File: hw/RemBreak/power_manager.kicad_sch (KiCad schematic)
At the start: 20 parts, among them IC1 LTC2943IDD#TRPBF, J4 Screw_Terminal_01x02, J5 Conn_01x03_MountingPin, Q1 BC337, Q2 BC847, U1 INA219BxDCN, U2 MAX40200AUK

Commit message: routing in progress added new subsheet to easily swap signals at the control connector
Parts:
- renumbered J4 to J3, J5 to J4
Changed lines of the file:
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@@
 		(dnp no)
 		(fields_autoplaced yes)
-		(property "Reference" "#PWR013"
+		(property "Reference" "#PWR010"
 			(at 116.84 69.85 0)
 			(effects
@@
 			(project "RemBreak"
 				(path "/e6d4ae5b-c9d7-4cbe-b288-c929fdf55a75/65dd8b54-1c0a-4683-aa46-51c439d49612"
-					(reference "#PWR013")
+					(reference "#PWR010")
 					(unit 1)
 				)
@@
 		(dnp no)
 		(fields_autoplaced yes)
-		(property "Reference" "#PWR018"
+		(property "Reference" "#PWR015"
 			(at 212.09 146.05 0)
 			(effects
@@
 			(project "RemBreak"
 				(path "/e6d4ae5b-c9d7-4cbe-b288-c929fdf55a75/65dd8b54-1c0a-4683-aa46-51c439d49612"
-					(reference "#PWR018")
+					(reference "#PWR015")
 					(unit 1)
 				)
@@
 		(on_board yes)
 		(dnp no)
-		(property "Reference" "J4"
+		(property "Reference" "J3"
 			(at 23.622 78.74 0)
 			(effects
@@
 			(project "RemBreak"
 				(path "/e6d4ae5b-c9d7-4cbe-b288-c929fdf55a75/65dd8b54-1c0a-4683-aa46-51c439d49612"
-					(reference "J4")
+					(reference "J3")
 					(unit 1)
 				)
@@
 		(dnp no)
 		(fields_autoplaced yes)
-		(property "Reference" "#PWR015"
+		(property "Reference" "#PWR012"
 			(at 190.5 74.93 0)
 			(effects
@@
 			(project ""
 				(path "/e6d4ae5b-c9d7-4cbe-b288-c929fdf55a75/65dd8b54-1c0a-4683-aa46-51c439d49612"
-					(reference "#PWR015")
+					(reference "#PWR012")
 					(unit 1)
 				)
@@
 		(dnp no)
 		(fields_autoplaced yes)
-		(property "Reference" "#PWR016"
+		(property "Reference" "#PWR013"
 			(at 200.66 78.74 0)
 			(effects
@@
 			(project ""
 				(path "/e6d4ae5b-c9d7-4cbe-b288-c929fdf55a75/65dd8b54-1c0a-4683-aa46-51c439d49612"
-					(reference "#PWR016")
+					(reference "#PWR013")
 					(unit 1)
 				)
@@
 		(dnp no)
 		(fields_autoplaced yes)
-		(property "Reference" "#PWR011"
+		(property "Reference" "#PWR08"
 			(at 80.01 144.78 0)
 			(effects
@@
 			(project "RemBreak"
 				(path "/e6d4ae5b-c9d7-4cbe-b288-c929fdf55a75/65dd8b54-1c0a-4683-aa46-51c439d49612"
-					(reference "#PWR011")
+					(reference "#PWR08")
 					(unit 1)
 				)
@@
 		(dnp no)
 		(fields_autoplaced yes)
-		(property "Reference" "#PWR010"
+		(property "Reference" "#PWR07"
 			(at 60.96 54.61 0)
 			(effects
@@
 			(project "RemBreak"
 				(path "/e6d4ae5b-c9d7-4cbe-b288-c929fdf55a75/65dd8b54-1c0a-4683-aa46-51c439d49612"
-					(reference "#PWR010")
+					(reference "#PWR07")
 					(unit 1)
 				)
@@
 		(on_board yes)
 		(dnp no)
-		(property "Reference" "J5"
+		(property "Reference" "J4"
 			(at 24.892 90.17 0)
 			(effects
@@
 			(project ""
 				(path "/e6d4ae5b-c9d7-4cbe-b288-c929fdf55a75/65dd8b54-1c0a-4683-aa46-51c439d49612"
-					(reference "J5")
+					(reference "J4")
 					(unit 1)
 				)
@@
 		(dnp no)
 		(fields_autoplaced yes)
-		(property "Reference" "#PWR09"
+		(property "Reference" "#PWR06"
 			(at 54.61 71.12 0)
 			(effects
@@
 			(project "RemBreak"
 				(path "/e6d4ae5b-c9d7-4cbe-b288-c929fdf55a75/65dd8b54-1c0a-4683-aa46-51c439d49612"
-					(reference "#PWR09")
+					(reference "#PWR06")
 					(unit 1)
 				)
@@
 		(dnp no)
 		(fields_autoplaced yes)
-		(property "Reference" "#PWR017"
+		(property "Reference" "#PWR014"
 			(at 207.01 34.29 0)
 			(effects
@@
 			(project "RemBreak"
 				(path "/e6d4ae5b-c9d7-4cbe-b288-c929fdf55a75/65dd8b54-1c0a-4683-aa46-51c439d49612"
-					(reference "#PWR017")
+					(reference "#PWR014")
 					(unit 1)
 				)
@@
 		(dnp no)
 		(fields_autoplaced yes)
-		(property "Reference" "#PWR014"
+		(property "Reference" "#PWR011"
 			(at 158.75 85.09 0)
 			(effects
@@
 			(project "RemBreak"
 				(path "/e6d4ae5b-c9d7-4cbe-b288-c929fdf55a75/65dd8b54-1c0a-4683-aa46-51c439d49612"
-					(reference "#PWR014")
+					(reference "#PWR011")
 					(unit 1)
 				)
@@
 		(dnp no)
 		(fields_autoplaced yes)
-		(property "Reference" "#PWR012"
+		(property "Reference" "#PWR09"
 			(at 92.71 124.46 0)
 			(effects
@@
 			(project "RemBreak"
 				(path "/e6d4ae5b-c9d7-4cbe-b288-c929fdf55a75/65dd8b54-1c0a-4683-aa46-51c439d49612"
-					(reference "#PWR012")
+					(reference "#PWR09")
 					(unit 1)
 				)
@@
 		(dnp no)
 		(fields_autoplaced yes)
-		(property "Reference" "#PWR07"
+		(property "Reference" "#PWR04"
 			(at 39.37 101.6 0)
 			(effects
@@
 			(project ""
 				(path "/e6d4ae5b-c9d7-4cbe-b288-c929fdf55a75/65dd8b54-1c0a-4683-aa46-51c439d49612"
-					(reference "#PWR07")
+					(reference "#PWR04")
 					(unit 1)
 				)
@@
 		(dnp no)
 		(fields_autoplaced yes)
-		(property "Reference" "#PWR08"
+		(property "Reference" "#PWR05"
 			(at 41.91 134.62 0)
 			(effects
@@
 			(project "RemBreak"
 				(path "/e6d4ae5b-c9d7-4cbe-b288-c929fdf55a75/65dd8b54-1c0a-4683-aa46-51c439d49612"
-					(reference "#PWR08")
+					(reference "#PWR05")
 					(unit 1)
 				)
@@
 		(dnp no)
 		(fields_autoplaced yes)
-		(property "Reference" "#PWR019"
+		(property "Reference" "#PWR016"
 			(at 236.22 146.05 0)
 			(effects
@@
 			(project "RemBreak"
 				(path "/e6d4ae5b-c9d7-4cbe-b288-c929fdf55a75/65dd8b54-1c0a-4683-aa46-51c439d49612"
-					(reference "#PWR019")
-					(unit 1)
-				)
+					(reference "#PWR016")
+					(unit 1)
+				)

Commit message: changed board settings and replaced r and c footprints with the ones for handsoldering
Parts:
- C1: footprint Capacitor_SMD:C_0805_2012Metric -> Capacitor_SMD:C_0805_2012Metric_Pad1.18x1.45mm_HandSolder
- R10, R11, R12, R13, R3, R4, R5, R7, R8, R9: footprint Resistor_SMD:R_0805_2012Metric -> Resistor_SMD:R_0805_2012Metric_Pad1.20x1.40mm_HandSolder
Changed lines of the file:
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@@
 			)
 		)
-		(property "Footprint" "Resistor_SMD:R_0805_2012Metric"
+		(property "Footprint" "Resistor_SMD:R_0805_2012Metric_Pad1.20x1.40mm_HandSolder"
 			(at 213.868 135.89 90)
 			(effects
@@
 			)
 		)
-		(property "Footprint" "Resistor_SMD:R_0805_2012Metric"
+		(property "Footprint" "Resistor_SMD:R_0805_2012Metric_Pad1.20x1.40mm_HandSolder"
 			(at 198.882 82.55 90)
 			(effects
@@
 			)
 		)
-		(property "Footprint" "Resistor_SMD:R_0805_2012Metric"
+		(property "Footprint" "Resistor_SMD:R_0805_2012Metric_Pad1.20x1.40mm_HandSolder"
 			(at 45.212 137.16 90)
 			(effects
@@
 			)
 		)
-		(property "Footprint" "Resistor_SMD:R_0805_2012Metric"
+		(property "Footprint" "Resistor_SMD:R_0805_2012Metric_Pad1.20x1.40mm_HandSolder"
 			(at 205.232 34.29 90)
 			(effects
@@
 			)
 		)
-		(property "Footprint" "Resistor_SMD:R_0805_2012Metric"
+		(property "Footprint" "Resistor_SMD:R_0805_2012Metric_Pad1.20x1.40mm_HandSolder"
 			(at 224.79 123.952 90)
 			(effects
@@
 			)
 		)
-		(property "Footprint" "Resistor_SMD:R_0805_2012Metric"
+		(property "Footprint" "Resistor_SMD:R_0805_2012Metric_Pad1.20x1.40mm_HandSolder"
 			(at 185.42 108.458 90)
 			(effects
@@
 			)
 		)
-		(property "Footprint" "Resistor_SMD:R_0805_2012Metric"
+		(property "Footprint" "Resistor_SMD:R_0805_2012Metric_Pad1.20x1.40mm_HandSolder"
 			(at 74.422 100.33 90)
 			(effects
@@
 			)
 		)
-		(property "Footprint" "Resistor_SMD:R_0805_2012Metric"
+		(property "Footprint" "Resistor_SMD:R_0805_2012Metric_Pad1.20x1.40mm_HandSolder"
 			(at 92.202 100.33 90)
 			(effects
@@
 			)
 		)
-		(property "Footprint" "Resistor_SMD:R_0805_2012Metric"
+		(property "Footprint" "Resistor_SMD:R_0805_2012Metric_Pad1.20x1.40mm_HandSolder"
 			(at 185.42 127.508 90)
 			(effects
@@
 			)
 		)
-		(property "Footprint" "Resistor_SMD:R_0805_2012Metric"
+		(property "Footprint" "Resistor_SMD:R_0805_2012Metric_Pad1.20x1.40mm_HandSolder"
 			(at 35.052 137.16 90)
 			(effects
@@
 			)
 		)
-		(property "Footprint" "Capacitor_SMD:C_0805_2012Metric"
+		(property "Footprint" "Capacitor_SMD:C_0805_2012Metric_Pad1.18x1.45mm_HandSolder"
 			(at 88.9 106.9848 0)
 			(effects

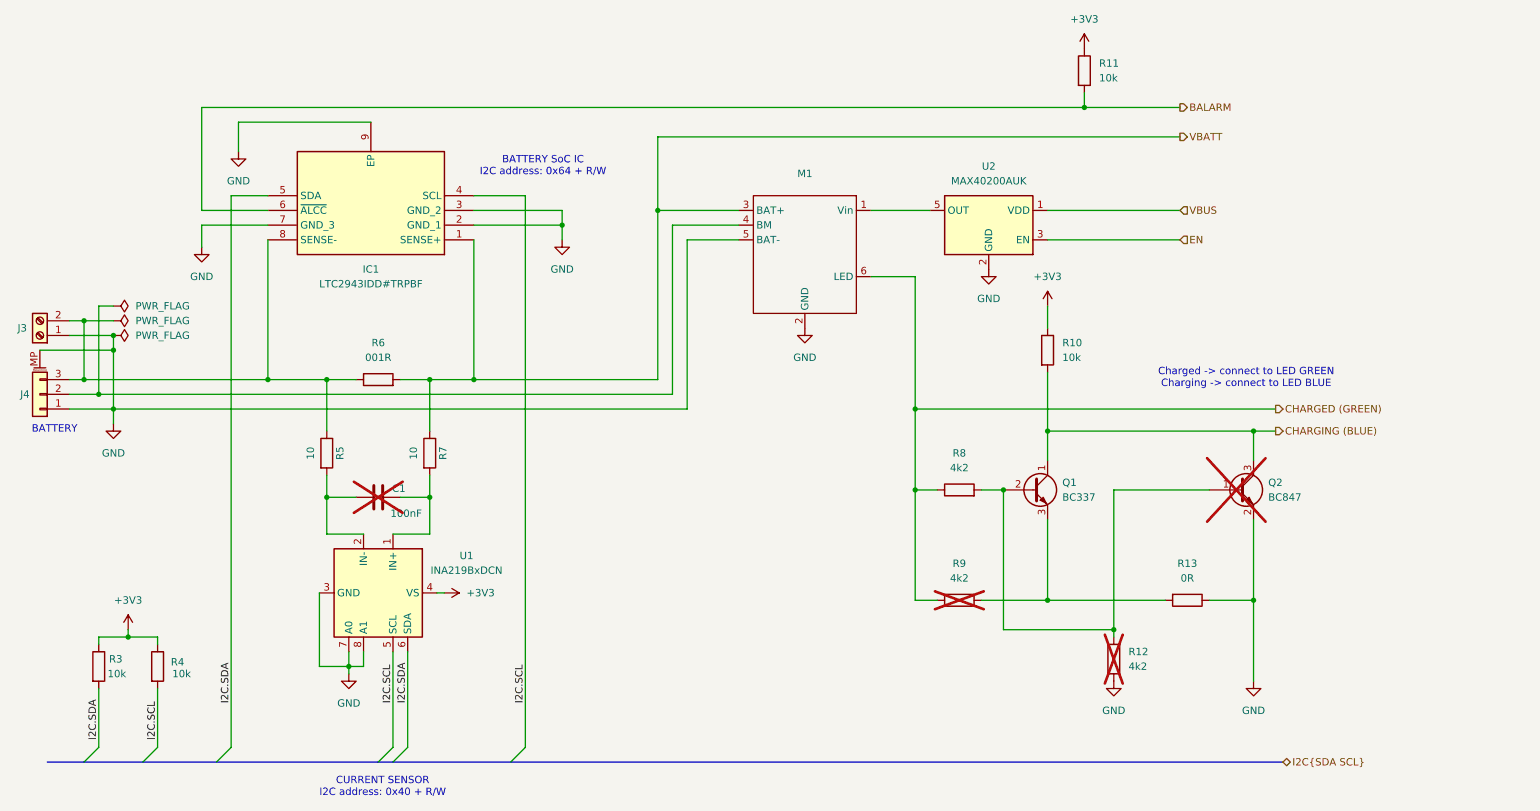
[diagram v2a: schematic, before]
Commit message: Note fonts changed to bold and added titles of the sheets included rev number
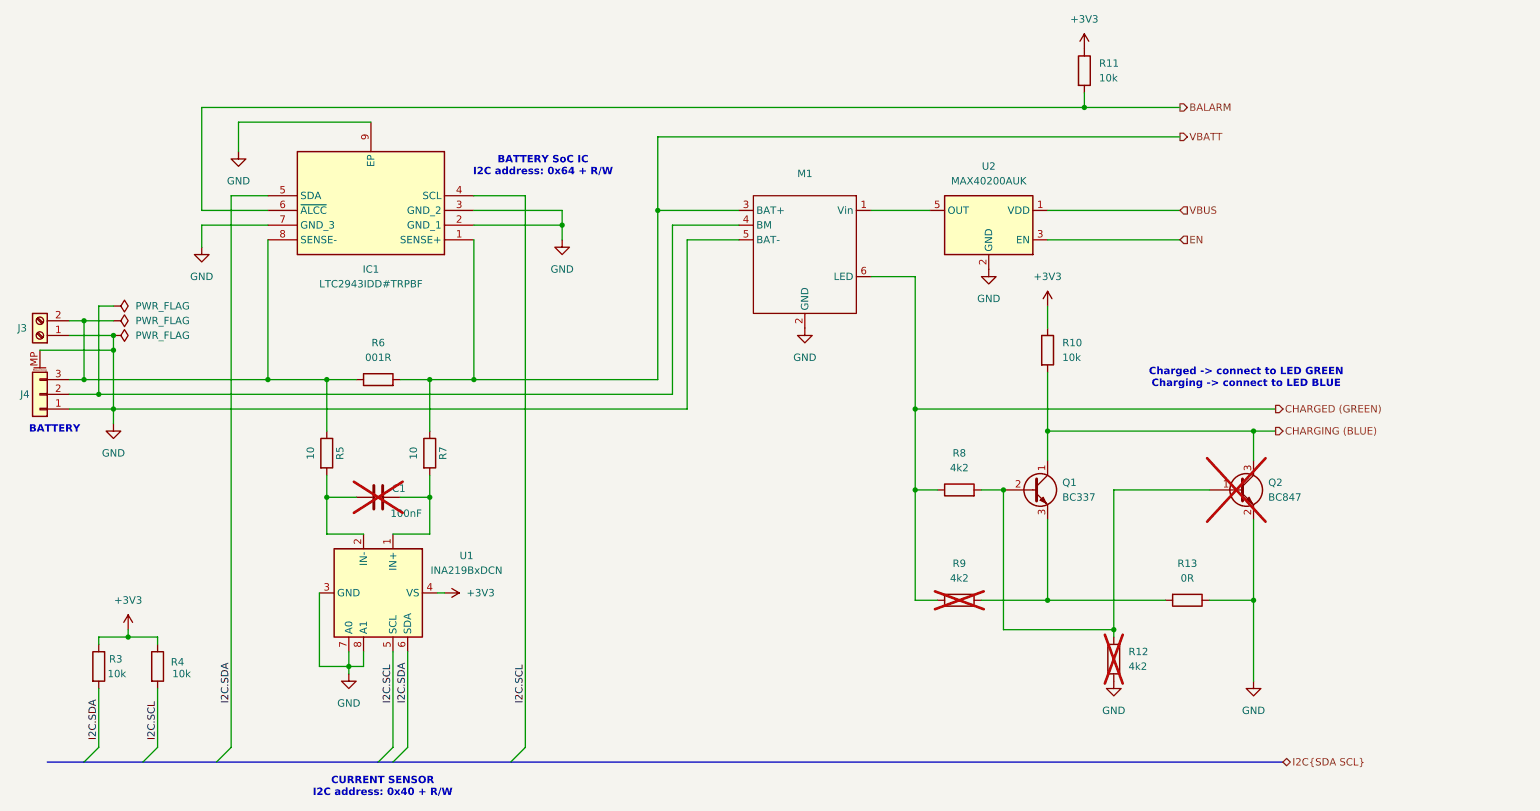
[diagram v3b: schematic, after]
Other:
- title: (none) -> Power Manager
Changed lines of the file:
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@@
 	(generator_version "8.99")
 	(paper "A4")
+	(title_block
+		(title "Power Manager")
+		(date "2024-12-15")
+		(rev "1.0")
+	)
 	(text "CURRENT SENSOR\nI2C address: 0x40 + R/W"
 		(exclude_from_sim no)
@@
 			(font
 				(size 1.27 1.27)
+				(thickness 0.254)
+				(bold yes)
 			)
 		)
@@
 			(font
 				(size 1.27 1.27)
+				(thickness 0.254)
+				(bold yes)
 			)
 		)
@@
 			(font
 				(size 1.27 1.27)
+				(thickness 0.254)
+				(bold yes)
 			)
 		)
@@
 			(font
 				(size 1.27 1.27)
+				(thickness 0.254)
+				(bold yes)
 			)
 		)
